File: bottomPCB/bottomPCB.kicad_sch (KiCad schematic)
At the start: 46 parts, among them J1 Conn_01x03_Pin, J2 Conn_02x03_Odd_Even, J3 Conn_01x02, J4 Conn_02x03_Odd_Even, J5 1-84953-1, J6 1-84953-1, J7 1-84953-1, J8 1-84953-1, U1 ESP32-WROOM-32, U2 XT30_horizontal, U8 LM1117IMPX-3_3_NOPB, U9 LM1117IMPX-3_3_NOPB

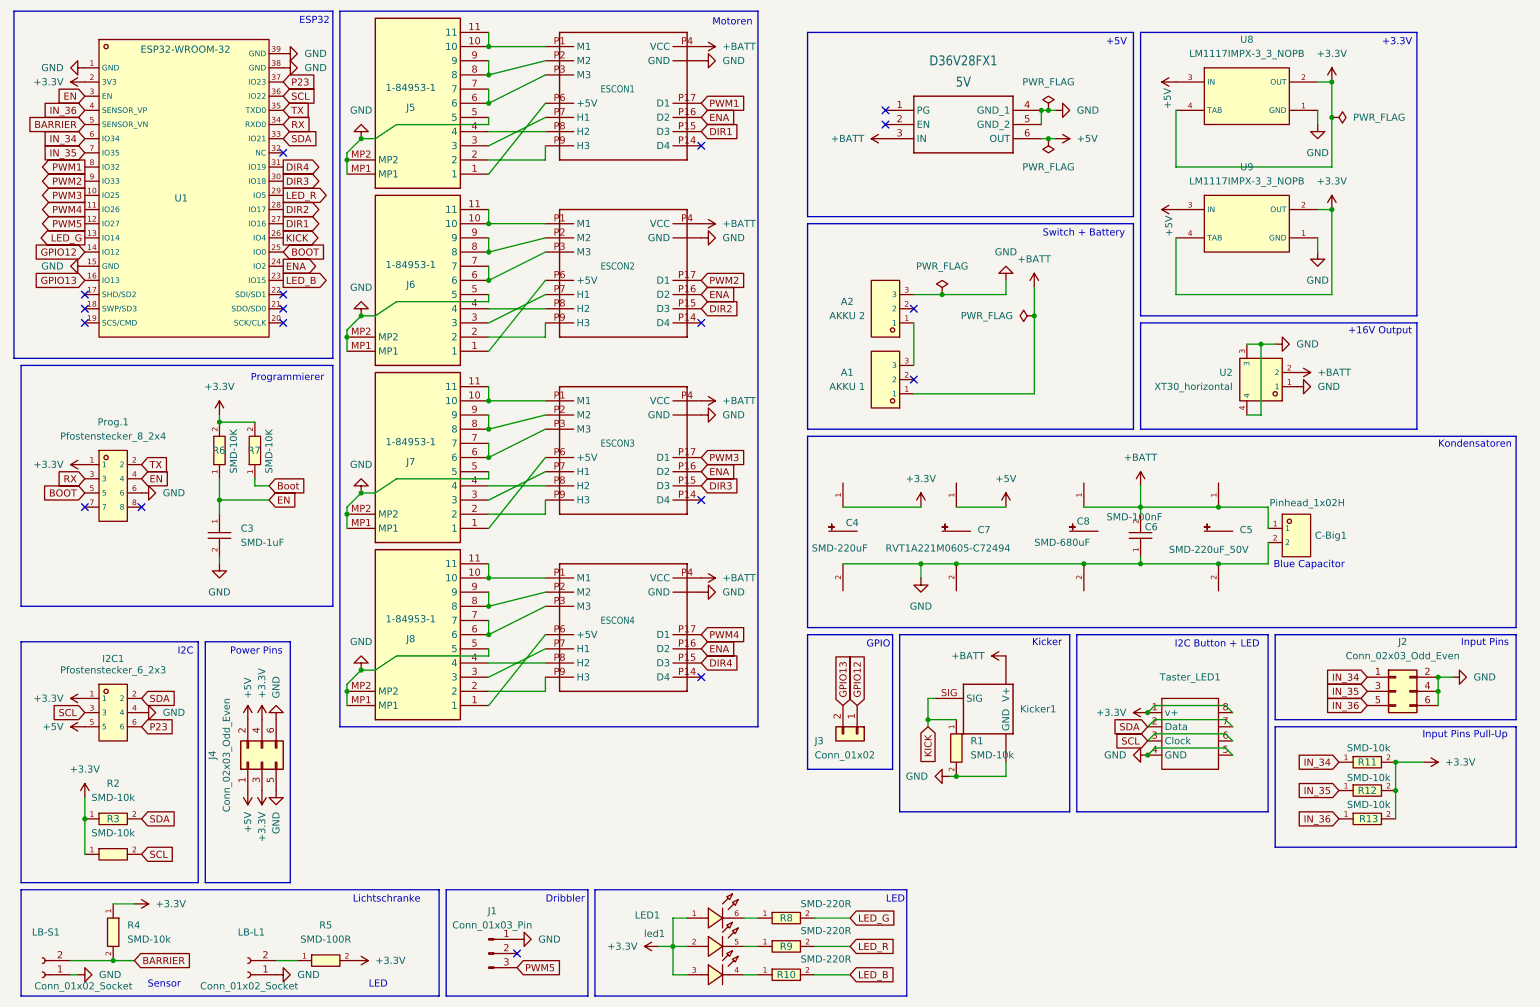
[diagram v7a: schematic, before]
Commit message: draft of pcb outline + placement of electronics
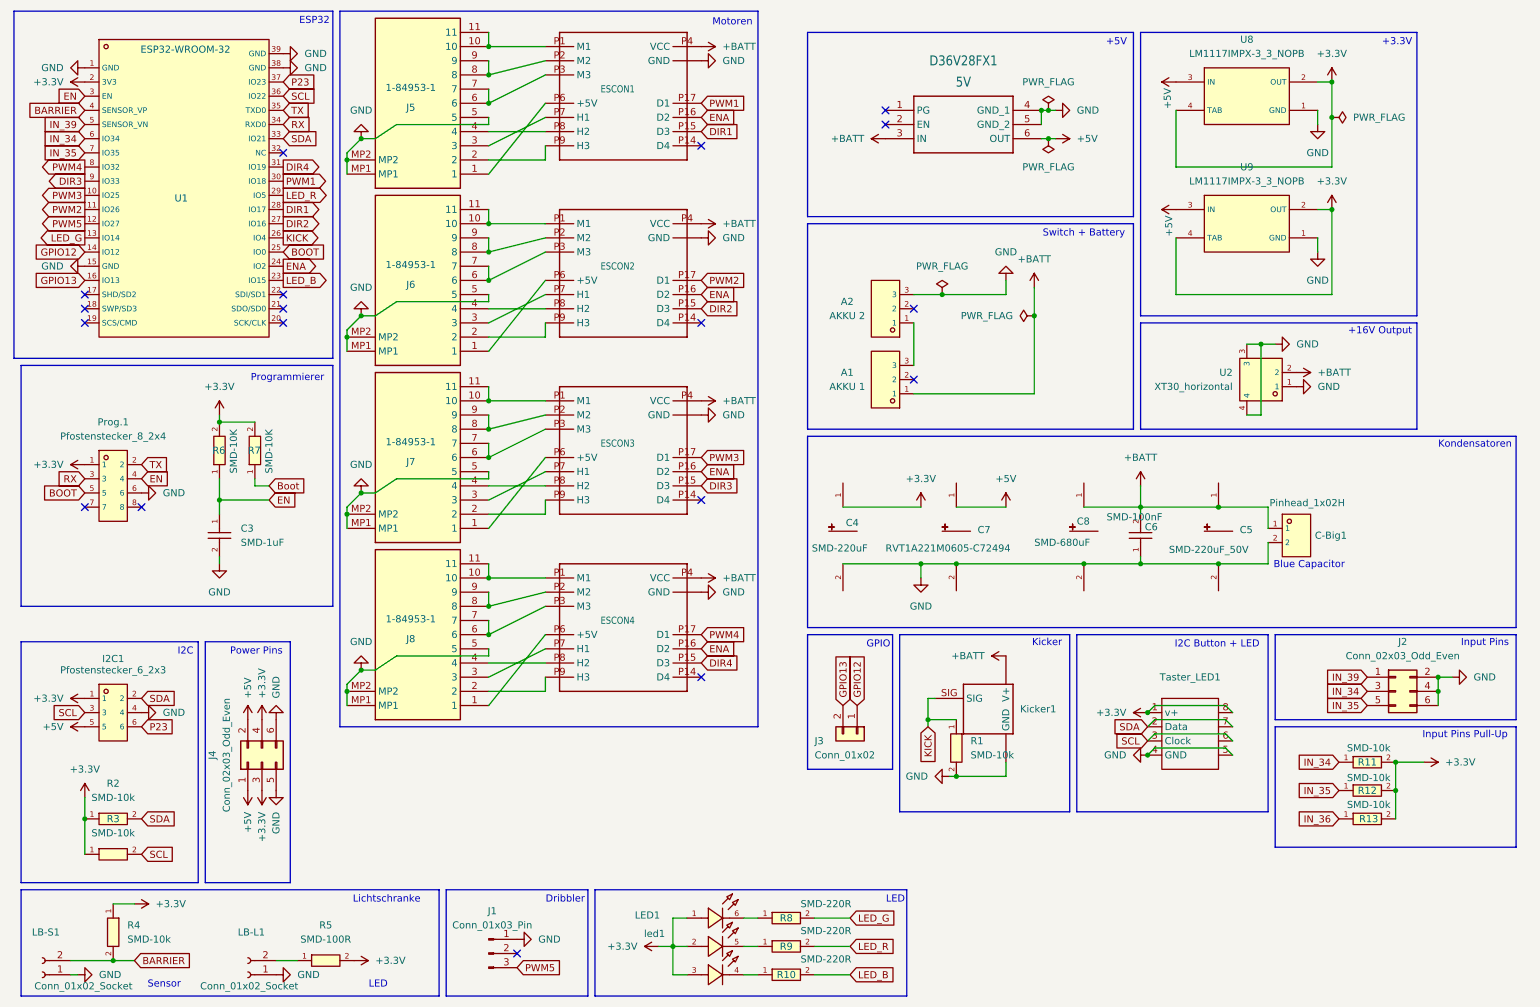
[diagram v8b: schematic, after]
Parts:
- J1: footprint (none) -> Connector_PinSocket_2.54mm:PinSocket_1x03_P2.54mm_Vertical
- J2, J4: footprint (none) -> Connector_PinSocket_2.54mm:PinSocket_2x03_P2.54mm_Vertical
- J3: footprint (none) -> Connector_PinSocket_2.54mm:PinSocket_1x02_P2.54mm_Vertical
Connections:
- net BARRIER: now also U1.4 (SENSOR_VP); no longer U1.5 (SENSOR_VN)
- net DIR1: now also U1.28 (IO17); no longer U1.27 (IO16)
- net DIR2: now also U1.27 (IO16); no longer U1.28 (IO17)
- net DIR3: now also U1.9 (IO33); no longer U1.30 (IO18)
- net IN_34: now also J2.3 (Pin_3); no longer J2.1 (Pin_1)
- net IN_35: now also J2.5 (Pin_5); no longer J2.3 (Pin_3)
- net IN_36: no longer J2.5 (Pin_5), U1.4 (SENSOR_VP)
- net PWM1: now also U1.30 (IO18); no longer U1.8 (IO32)
- net PWM2: now also U1.11 (IO26); no longer U1.9 (IO33)
- net PWM4: now also U1.8 (IO32); no longer U1.11 (IO26)
- new net IN_39: J2.1 (Pin_1), U1.5 (SENSOR_VN)
